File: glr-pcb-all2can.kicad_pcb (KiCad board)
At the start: 4 copper layers, 64 x 40 mm, 90 parts, among them IC1 ATA6561-GAQW-N, IC2 ZMR330FTA, IC3 AP64060WU-7, IC4 STM32C092KCT6, IC5 LSM6DSV16BXTR, J1 DA15_Pins_MountingHoles, J3 Conn_01x04, J4 Conn_01x02, J5 Conn_01x02, J6 62701021621, Q1 DMN6075S, Q2 DMN6075S, Q3 DMN6075S, Q4 DMN6075S

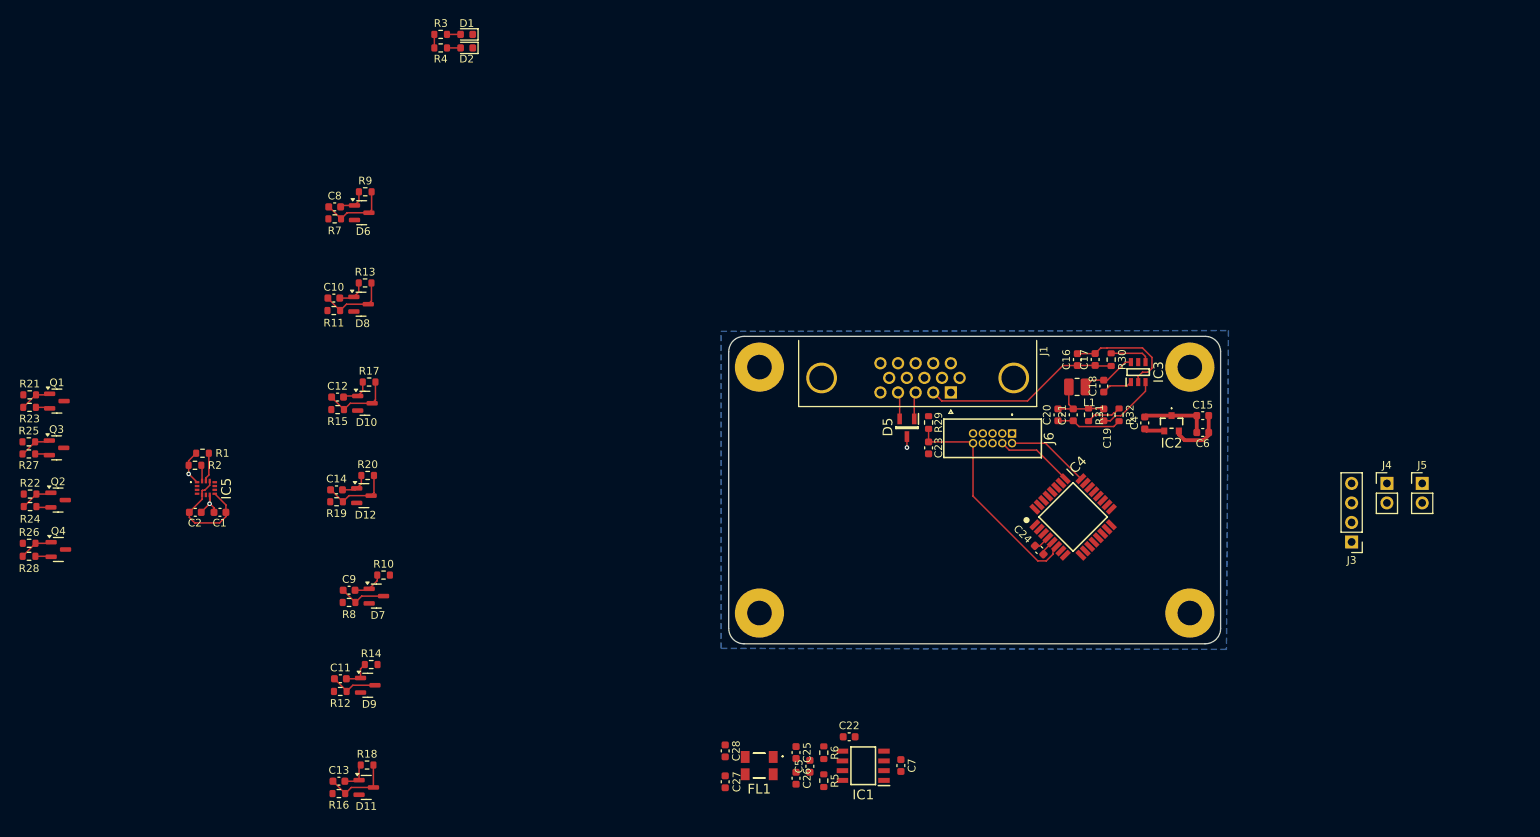
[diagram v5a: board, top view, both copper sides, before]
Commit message: reorder more
move pullup i2c in schematic
make power passing routes thicker
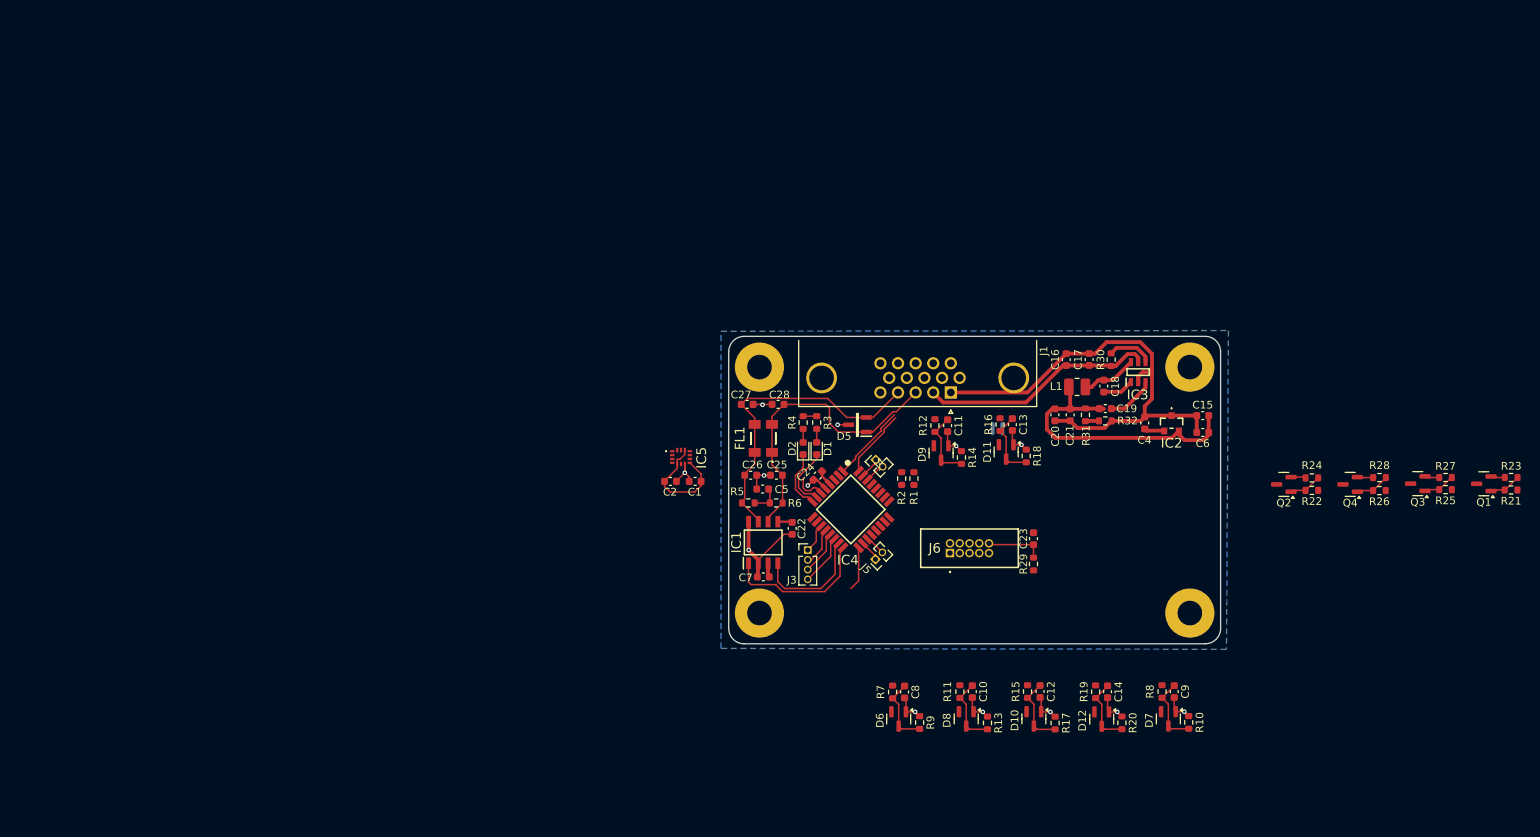
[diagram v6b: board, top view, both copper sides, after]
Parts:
- J3: footprint Connector_PinHeader_2.54mm:PinHeader_1x04_P2.54mm_Vertical -> Connector_PinHeader_1.27mm:PinHeader_1x04_P1.27mm_Vertical
- J4, J5: footprint Connector_PinHeader_2.54mm:PinHeader_1x02_P2.54mm_Vertical -> Connector_PinHeader_1.27mm:PinHeader_1x02_P1.27mm_Vertical
- moved R21 193.1 mm to (219.8, 110.0), turned to 180 degrees
- moved R23 193.0 mm to (219.8, 108.4), turned to 180 degrees
- moved Q1 186.0 mm to (216.3, 109.2), turned to 180 degrees
- moved R25 184.4 mm to (211.3, 109.9), turned to 180 degrees
- moved R27 184.4 mm to (211.3, 108.4), turned to 180 degrees
- moved Q3 177.2 mm to (207.7, 109.2), turned to 180 degrees
- moved R28 176.0 mm to (202.7, 108.4), turned to 180 degrees
- moved R26 175.8 mm to (202.7, 110.1), turned to 180 degrees
- moved Q4 168.3 mm to (198.9, 109.3), turned to 180 degrees
- moved R24 166.8 mm to (193.9, 108.4), turned to 180 degrees
- moved R22 166.8 mm to (193.9, 110.0), turned to 180 degrees
- moved Q2 159.5 mm to (190.2, 109.3), turned to 180 degrees
- moved C9 108.2 mm to (176.0, 136.2), turned to -90 degrees
- moved R10 106.5 mm to (177.9, 140.2), turned to -90 degrees
- moved R8 106.4 mm to (174.4, 136.2), turned to -90 degrees
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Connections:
- R1 pad 2: I2C1_SCL -> I2C1_SDA
- R2 pad 2: I2C1_SDA -> I2C1_SCL
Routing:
- net GND: track 81.3 -> 129.9 mm, vias 3 -> 13
- net /CAN transciever/CAN H 1: track 3.53 -> 41.0 mm
- net /CAN transciever/CAN L 1: track 3.51 -> 39.2 mm
- net +5V: track 16.5 -> 39.9 mm
- net FDCAN1_TX: track 0.00 -> 19.6 mm
- net NRST: track 29.9 -> 11.8 mm
- net FDCAN1_RX: track 0.00 -> 15.2 mm
- net IC_IN_6: track 6.33 -> 18.1 mm
- net SWDIO: track 10.9 -> 0.00 mm
- net SWCLK: track 10.2 -> 0.12 mm
- net IC_IN_7: track 9.35 -> 19.3 mm
- net LED_1: track 0.00 -> 8.59 mm
- net IC_IN_5: track 6.26 -> 14.8 mm
- net LED_2: track 0.00 -> 8.21 mm
- net SPI1_MOSI: track 0.00 -> 6.68 mm
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
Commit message: almost route everything
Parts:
- G***: moved to F.Cu
- moved Q4 47.8 mm to (151.0, 109.7)
- moved R26 47.8 mm to (154.8, 110.5)
- moved R28 47.8 mm to (154.8, 108.8)
- moved R23 40.6 mm to (179.2, 108.8)
- moved Q1 40.6 mm to (175.6, 109.6)
- moved R21 40.6 mm to (179.2, 110.4)
- moved R25 40.1 mm to (171.1, 110.4)
- moved Q3 40.1 mm to (167.5, 109.6)
- moved R27 40.1 mm to (171.1, 108.8)
- moved C2 36.5 mm to (146.9, 110.4), turned to -135 degrees
- moved C1 32.1 mm to (145.7, 109.3), turned to 45 degrees
- moved IC5 31.8 mm to (143.6, 107.0), turned to -45 degrees
- moved Q2 30.9 mm to (159.4, 109.7)
- moved R22 30.9 mm to (163.0, 110.5)
- moved R24 30.9 mm to (163.0, 108.9)
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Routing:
- net +5V: track 39.9 -> 163.3 mm, vias 0 -> 4
- net +3V3: track 23.4 -> 131.4 mm, vias 0 -> 6
- net /Input filter/5_IN: track 0.00 -> 56.3 mm, vias 0 -> 4
- net /Output/1_OUT: track 0.00 -> 51.6 mm, vias 0 -> 2
- net /Input filter/4_IN: track 0.00 -> 47.7 mm, vias 0 -> 4
- net IC_OUT_1: track 0.00 -> 45.4 mm
- net /Output/2_OUT: track 0.00 -> 42.2 mm, vias 0 -> 2
- net IC_IN_5: track 14.8 -> 55.1 mm
- net IC_OUT_2: track 0.00 -> 37.6 mm
- net IC_IN_4: track 9.24 -> 46.4 mm
- net /Input filter/3_IN: track 0.00 -> 31.9 mm, vias 0 -> 4
- net /Output/3_OUT: track 0.00 -> 31.7 mm, vias 0 -> 3
- net IC_OUT_3: track 0.00 -> 29.8 mm
- net SWCLK: track 0.12 -> 29.3 mm, vias 0 -> 2
- net IC_IN_3: track 9.25 -> 37.4 mm
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
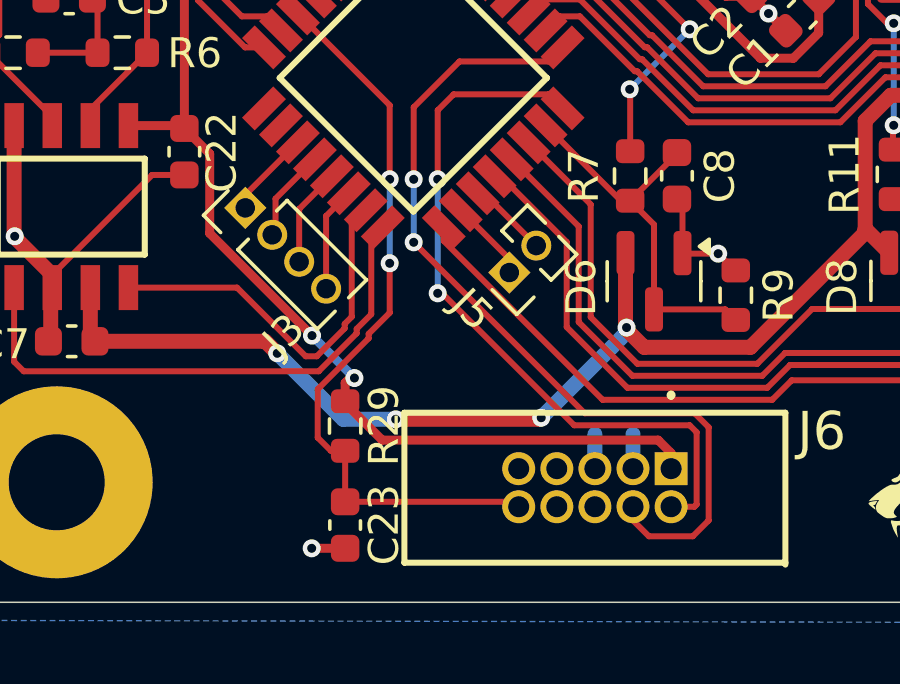
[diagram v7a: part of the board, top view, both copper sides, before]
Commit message: add missing pull down resistor for swd
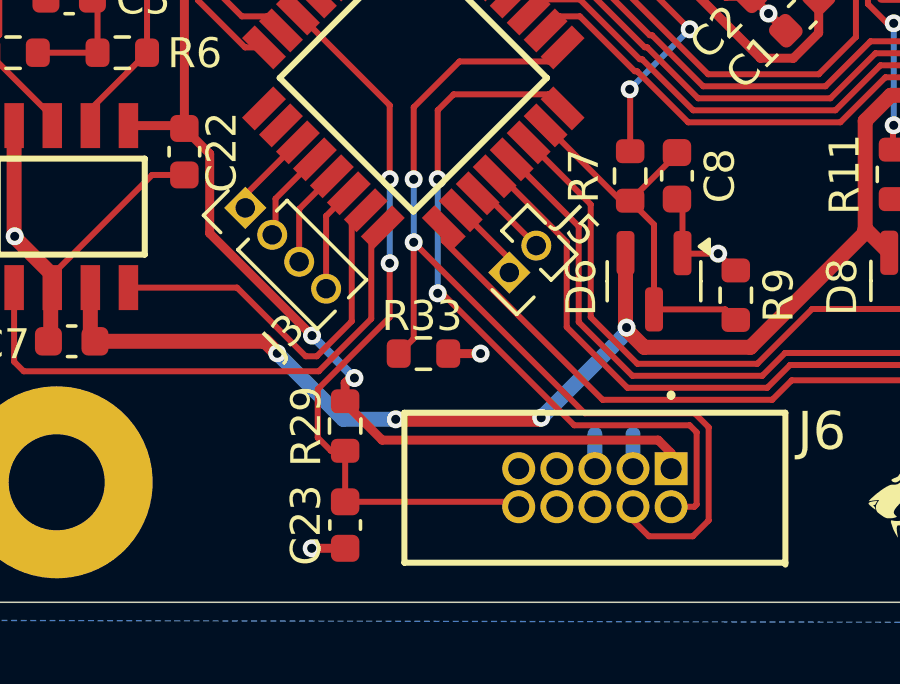
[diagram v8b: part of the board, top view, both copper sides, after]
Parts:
- added R33: 100k, Resistor_SMD:R_0603_1608Metric, F.Cu at (134.2, 121.7)
- turned R29 to -90 degrees
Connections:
- R29 pad 1: NRST -> +3V3
- R29 pad 2: +3V3 -> NRST
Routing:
- net SWCLK: track 29.3 -> 33.2 mm
- net GND: track 143.4 -> 144.5 mm, vias 21 -> 22
